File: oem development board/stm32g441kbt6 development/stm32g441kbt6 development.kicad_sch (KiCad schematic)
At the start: 53 parts, among them J1 CONN_pcie_x1, J2 Programming_Pin_Header, SW1 INTERRUPT TEST SWITCH, U1 STM32G441KBT6, U2 MCP2561-E_SN, U3 AP63203WU-7, Y1 X_Crystal_16MHz_18pF

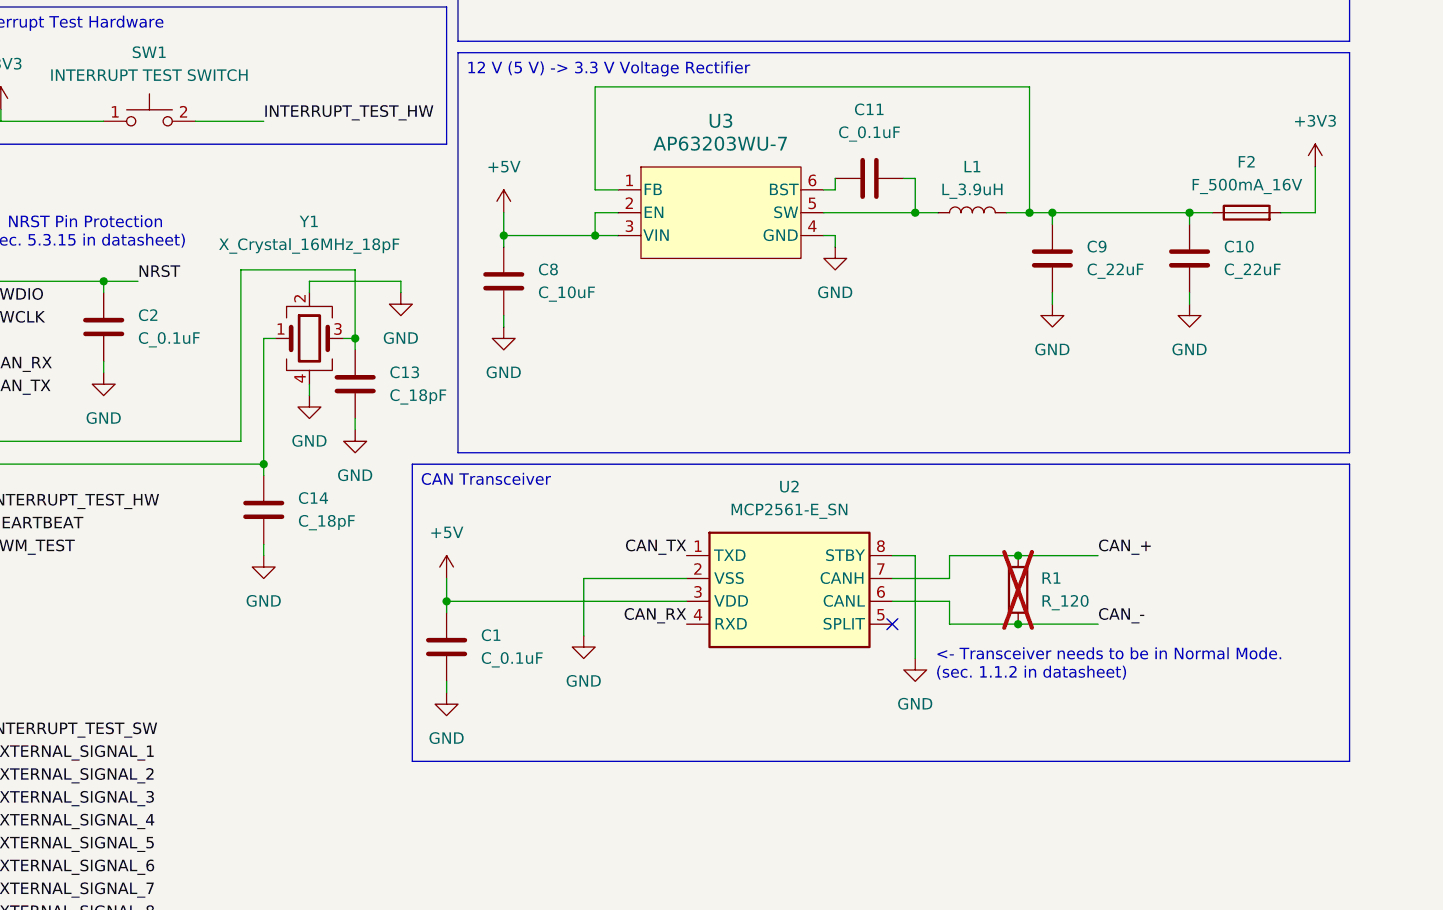
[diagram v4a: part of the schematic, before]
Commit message: Added Datasheet References, Minor PCB Design Changes
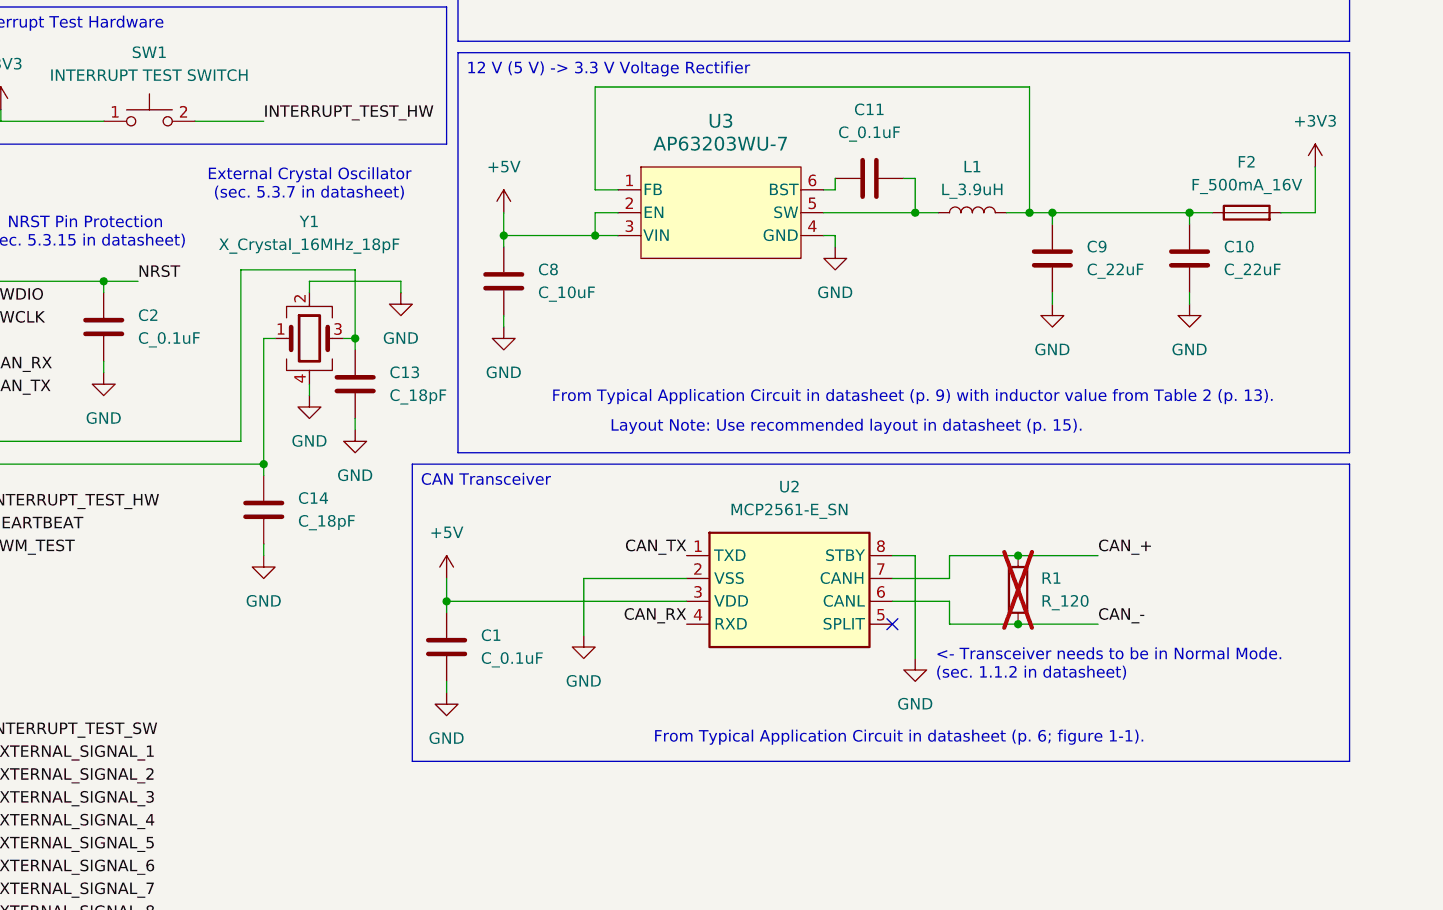
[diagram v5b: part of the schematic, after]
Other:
- note added: "External Crystal Oscillator (sec. 5.3.7 in datasheet)"
- note added: "From Typical Application Circuit in datasheet (p. 6; figure 1-1)."
- note added: "From Typical Application Circuit in datasheet (p. 9) with inductor value from Table 2 (p. 13)."
- note added: "Layout Note: Use recommended layout in datasheet (p. 15)."
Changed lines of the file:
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@@
+		)
+	)
+	(text "Layout Note: Use recommended layout in datasheet (p. 15)."
+		(exclude_from_sim no)
+		(at 228.6 128.016 0)
+		(effects
+			(font
+				(size 1.27 1.27)
+			)
 		)
 	)
@@
 		(exclude_from_sim no)
 		(at 199.136 28.956 0)
+		(effects
+			(font
+				(size 1.27 1.27)
+			)
+		)
+	)
+	(text "From Typical Application Circuit in datasheet (p. 6; figure 1-1)."
+		(exclude_from_sim no)
+		(at 234.442 162.56 0)
 		(effects
 			(font
@@
 		)
 	)
+	(text "External Crystal Oscillator\n(sec. 5.3.7 in datasheet)"
+		(exclude_from_sim no)
+		(at 168.91 101.092 0)
+		(effects
+			(font
+				(size 1.27 1.27)
+			)
+		)
+	)
 	(text "Layout Note: Each 0.1 uF capacitor\ncorresponds to one VDD pin."
 		(exclude_from_sim no)
@@
 		(effects
 			(font
+				(size 1.27 1.27)
+			)
+		)
+	)
+	(text "From Typical Application Circuit in datasheet (p. 9) with inductor value from Table 2 (p. 13)."
+		(exclude_from_sim no)
+		(at 235.966 124.714 0)
+		(effects
+			(font

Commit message: Changed Crystal Oscillator Load Capacitors to 30 pF from 18 pF (this should provide the manufacturer's specified load capacitance)
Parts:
- removed C13, C14: C_18pF, Capacitor_SMD:C_0805_2012Metric, symbol OEM:C_18pF
- added C13, C14: C_30pF, OEM:C_0603, symbol OEM:C_30pF
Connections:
- net GND: now also C13.2, C14.2
- net at U1.2 (PF0-OSC_IN), Y1.3: now also C13.1
- net at U1.3 (PF1-OSC_OUT), Y1.1: now also C14.1
